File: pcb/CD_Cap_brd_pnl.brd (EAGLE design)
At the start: 160 x 100 mm, 20 parts, among them Q1 IRF3704S, Q2 IRF3704S, U1 TC4422AVOA

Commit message: finished the circuits etc.
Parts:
- removed ARDUINO: ARDUINO_PRO_MINI, SparkFun-Boards:ARDUINO_PRO_MINI
- removed C1: 1uF, passives-7351:C0805-N
- removed C2, C3: 0.1uF, passives-7351:C0603-N
- removed C4: (no value), passives-7351:C0603-N
- removed C5: 0.015uF, passives-7351:C0603-N
- removed R1: 10k, passives-7351:R0603-N
- removed R2: 1k, passives-7351:R0603-N
- removed U1: TC4422AVOA, Microchip_By_element14_Batch_1:SOIC127P600X175-8N
- added J3, J4: (no value), SparkFun-Connectors:1X03_LOCK
- added U$1, U$2, U$3, U$4: BIG_PINHEADX110-32, _my-parts:M6_PINHEAD
- moved J1 237.1 mm to (100.3, 32.4)
- moved J2 218.9 mm to (100.3, 5.71)
- moved C8 174.0 mm to (64.8, 10.2), flipped to the bottom, turned to 270 degrees
- moved C7 146.7 mm to (34.3, 29.2), flipped to the bottom, turned to 270 degrees
- moved R5 145.3 mm to (99.7, 29.8)
- moved R3 141.4 mm to (97.8, 33.0), turned to 270 degrees
- moved R6 138.3 mm to (101.6, 8.26), turned to 180 degrees
- moved R4 137.7 mm to (99.7, 18.4), turned to 180 degrees
- moved Q2 137.0 mm to (108.0, 24.8), turned to 270 degrees
- moved Q1 121.1 mm to (108.0, 13.3), turned to 270 degrees
- moved C6 87.0 mm to (3.81, 11.4), flipped to the bottom, turned to 270 degrees
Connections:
- removed net 5V: ARDUINO.21
- removed net 9V: ARDUINO.24
- removed net CAP_V_READ: ARDUINO.17
- removed net ENC_01: ARDUINO.9
- removed net ENC_02: ARDUINO.10
- removed net ENC_11: ARDUINO.5
- removed net ENC_12: ARDUINO.6
- removed net ENC_21: ARDUINO.7
- removed net ENC_22: ARDUINO.8
- removed net GND: ARDUINO.23, C1.2, C2.2, C3.2, C4.1, C5.2, Q1.1, Q1.3, Q2.3, R1.1, R4.2, R6.1, R6.2, U1.4, U1.5
- removed net N$12: ARDUINO.16
- removed net N$13: ARDUINO.15
- removed net N$14: ARDUINO.14
- removed net N$15: ARDUINO.13
- removed net N$19: ARDUINO.18
- removed net N$2: C1.1, C2.1, C3.1, U1.1, U1.8
- removed net N$3: R1.2, R2.1, U1.2
- removed net N$5: R5.2
- removed net SW: ARDUINO.11
- removed net TRIG_5V: ARDUINO.12, R2.2
- new net D: Q1.2, Q2.2, U$3.P$1, U$4.P$1
- new net N$1: Q1.1, R4.2, R6.1
- net B+: now also U$1.P$1, U$2.P$1
- net B-: now also J1.1, J2.1, J3.1, J3.2, J3.3, J4.1, J4.2, J4.3, Q1.3, Q2.3, R5.2, R6.2; no longer J1.2, J2.2, Q1.2, Q2.2
- net TRIG: now also J1.2, J2.2; no longer C4.2, C5.1, J1.1, J2.1, U1.6, U1.7
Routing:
- net B+: track 0.00 -> 43.1 mm
- net TRIG: track 0.00 -> 37.2 mm, vias 0 -> 1
- net B-: track 0.00 -> 15.5 mm, vias 0 -> 3
- net N$1: track 0.00 -> 15.0 mm
- net N$4: track 0.00 -> 5.44 mm
- added copper zone on layer 1, net B+
- added copper zone on layer 1, net B-
- added copper zone on layer 16, net B-
- added copper zone on layer 1, net D
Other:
- board size 160 x 100 mm -> 128 x 39.4 mm

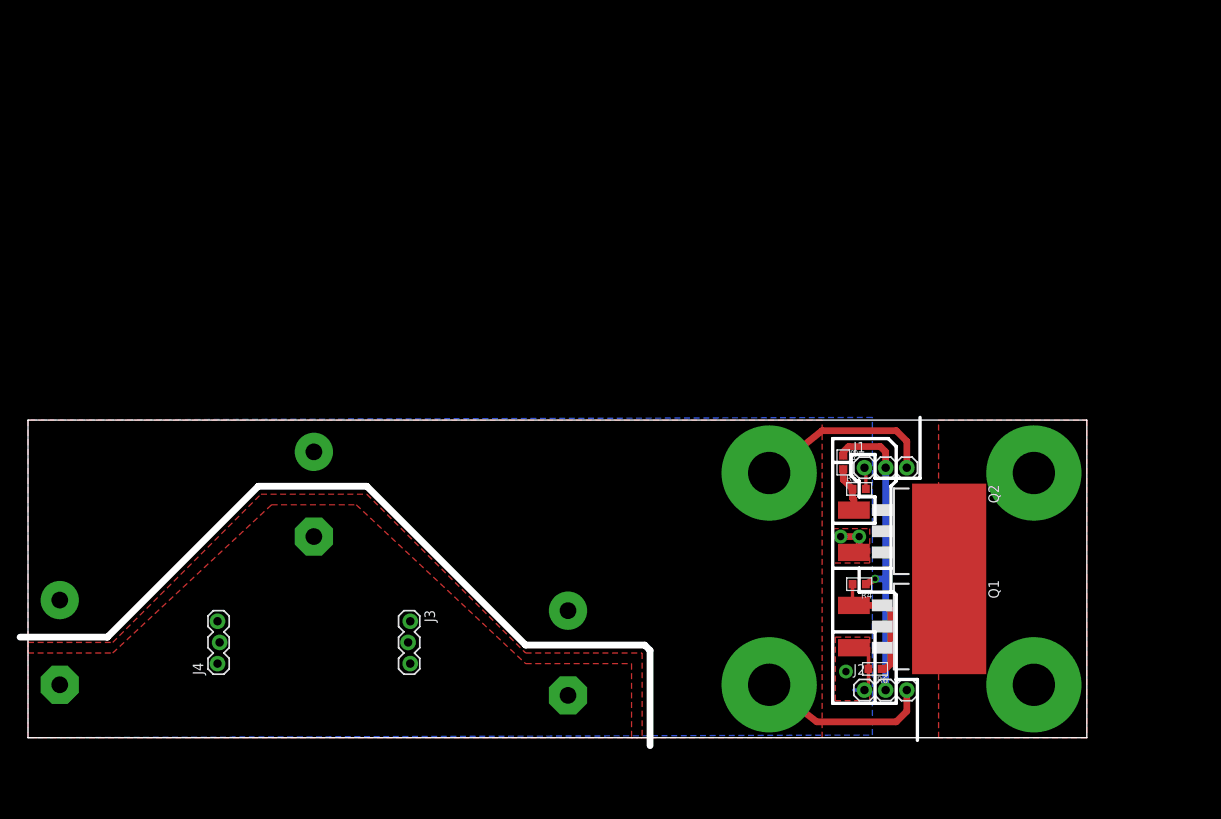
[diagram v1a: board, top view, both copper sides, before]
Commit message: fixed CD BRAINS Inconsistencies
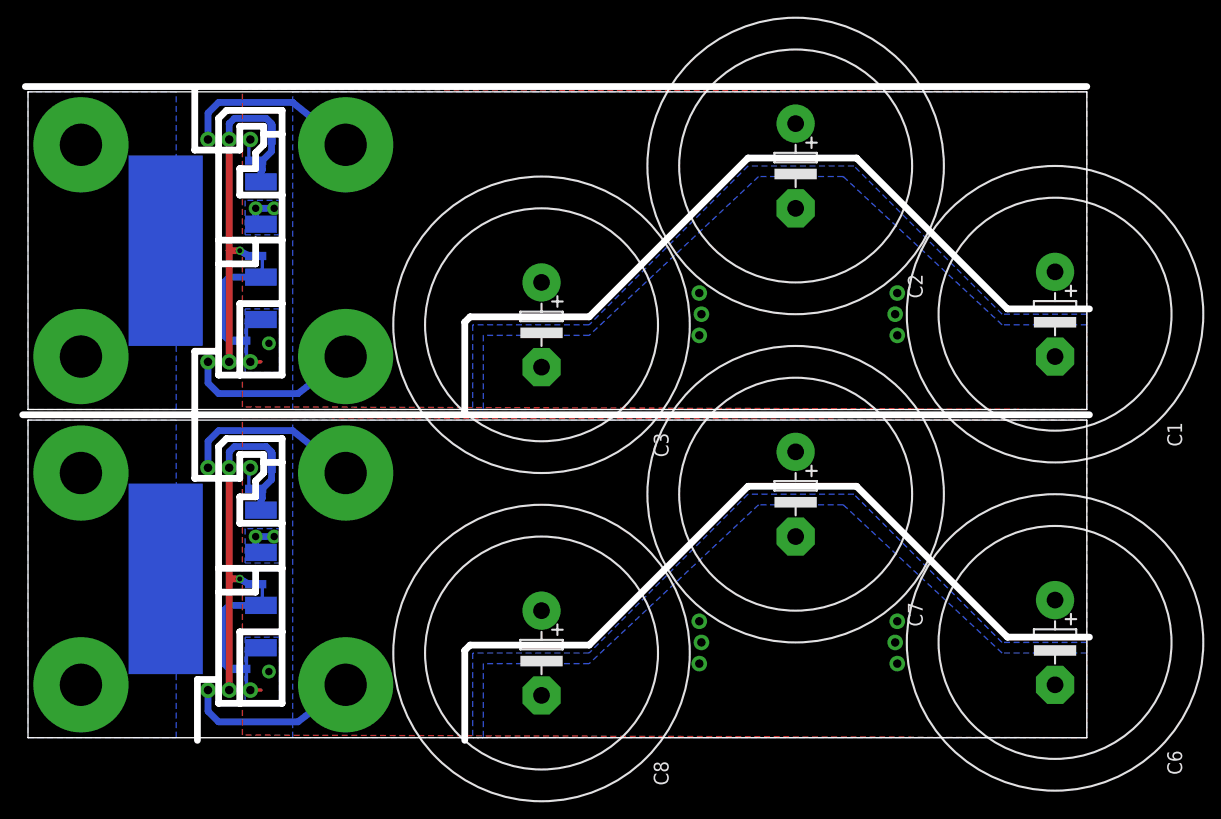
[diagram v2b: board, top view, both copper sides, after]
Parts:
- added C1, C2, C3: (no value), resistor:EB35D
- added J5, J6: (no value), SparkFun-Connectors:1X03
- added J7, J8: (no value), SparkFun-Connectors:1X03_LOCK
- added Q3, Q4: IRF3704S, transistor-power:D2PACK
- added R1, R2: 100, passives-7351:R0603-N
- added R7, R8: 10k, passives-7351:R0603-N
- added U$5, U$6, U$7, U$8: BIG_PINHEADX110-32, _my-parts:M6_PINHEAD
- moved C6 119.4 mm to (123.2, 11.4), flipped to the top
- moved U$3 114.3 mm to (6.35, 31.8), flipped to the bottom
- moved U$4 114.3 mm to (6.35, 6.35), flipped to the bottom
- moved Q1 88.9 mm to (19.1, 13.3), flipped to the bottom
- moved Q2 88.9 mm to (19.1, 24.8), flipped to the bottom
- moved J4 81.3 mm to (104.1, 8.89), flipped to the bottom
- moved R6 76.2 mm to (25.4, 8.26), flipped to the bottom
- moved J1 73.7 mm to (26.7, 32.4), flipped to the bottom
- moved J2 73.7 mm to (26.7, 5.71), flipped to the bottom
- moved R4 72.4 mm to (27.3, 18.4), flipped to the bottom
- moved R5 72.4 mm to (27.3, 29.8), flipped to the bottom
- moved R3 68.6 mm to (29.2, 33.0), flipped to the bottom
- moved C7 57.8 mm to (92.1, 29.2), flipped to the top
- moved U$1 50.8 mm to (38.1, 31.8), flipped to the bottom
- moved U$2 50.8 mm to (38.1, 6.35), flipped to the bottom
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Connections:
- new net B+1: C1.+, C2.+, C3.+, J5.3, J6.3, U$5.P$1, U$6.P$1
- new net B-1: C1.-, C2.-, C3.-, J5.1, J6.1, J7.1, J7.2, J7.3, J8.1, J8.2, J8.3, Q3.3, Q4.3, R7.2, R8.2
- new net D1: Q3.2, Q4.2, U$7.P$1, U$8.P$1
- new net N$3: Q4.1, R1.2, R7.1
- new net N$5: Q3.1, R2.2, R8.1
- new net TRIG1: J5.2, J6.2, R1.1, R2.1
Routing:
- net B+1: track 0.00 -> 43.1 mm
- net TRIG1: track 0.00 -> 37.2 mm, vias 0 -> 1
- net B-1: track 0.00 -> 15.5 mm, vias 0 -> 3
- net N$5: track 0.00 -> 15.0 mm
- net N$3: track 0.00 -> 5.44 mm
- added copper zone on layer 16, net B+
- added copper zone on layer 16, net B+1
- added copper zone on layer 1, net B-1
- added copper zone on layer 16, net B-1
- added copper zone on layer 16, net D
- added copper zone on layer 16, net D1
- removed copper zone on layer 1, net B+
- removed copper zone on layer 1, net D
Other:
- board size 128 x 39.4 mm -> 128 x 78.4 mm
